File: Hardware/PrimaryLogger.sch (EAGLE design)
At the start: 91 parts, among them J1 CONN_42.54_SCREW, J2 CONN_42.54_SCREW, J3 CONN_42.54_SCREW, J4 CONN_42.54_SCREW, J5 CONN_32.54_SCREW, J9 GEMS_POWER_PLUGINPUT, Q1 DMG3404, Q2 DMG3404, U1 MIC2005, U10 TPL5010DDC, U11 MIC842, U12 PCA9617TSSOP8, U13 MCP23008SSOP, U2 MIC2005, U25 SN74AUP3G34DCU, U3 TPL5010DDC, U5 SN74LVC1G3157SC70, U6 TCS3400, U7 SHTC3DFN, U9 MCP7940SOIC

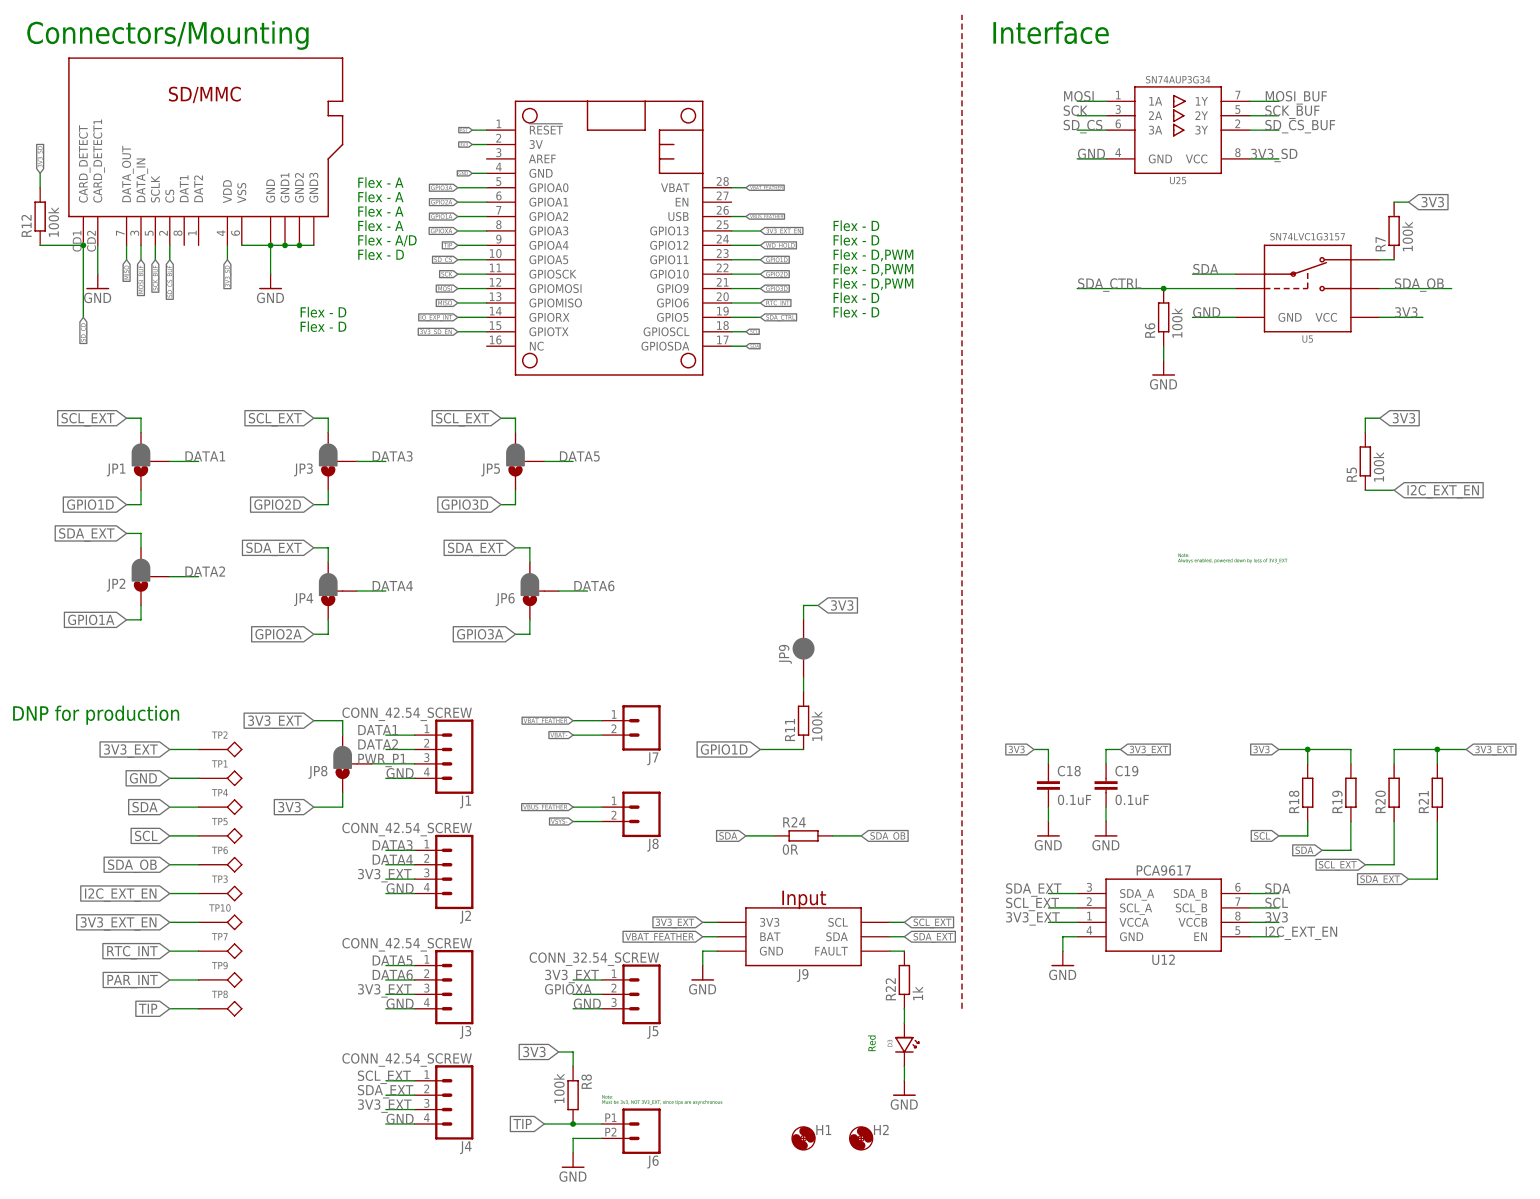
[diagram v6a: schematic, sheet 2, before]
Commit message: Cleanup and gerbers for v0.3A
Cleanup of schematic and layout for v0.3A design
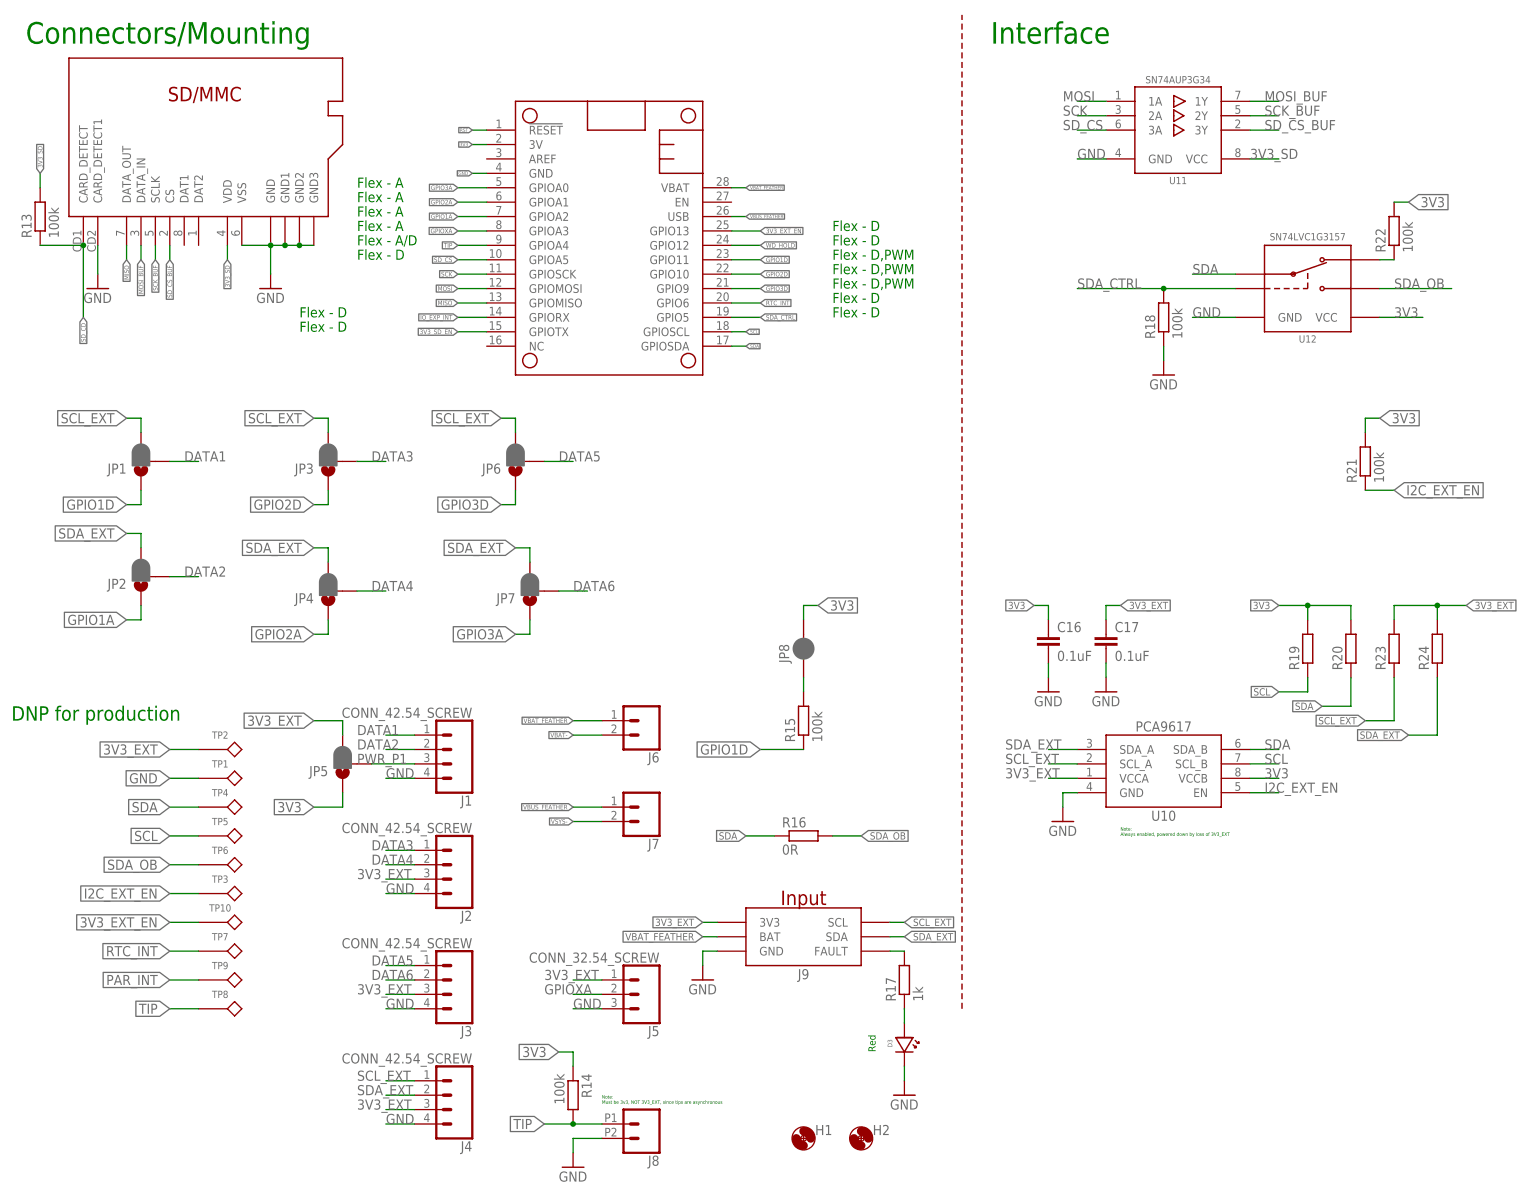
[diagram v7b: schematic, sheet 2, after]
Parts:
- removed C18, C19: 0.1uF, bschulz_passives:C-EU0.1UFC0603
- removed JP9: JUMPER-SMT_2_NC_PASTE_SILK, bschulz:JUMPER-SMT_2_NC_PASTE_SILK
- removed U13: MCP23008SSOP, bschulz:MCP23008SSOP
- removed U25: SN74AUP3G34DCU, bschulz:SN74AUP3G34DCU
- added C8, C9: 0.1uF, bschulz_passives:C-EU0.1UFC0603
- added JP7: JUMPER-SMT_3_1-NC_PASTE_SILK, bschulz:JUMPER-SMT_3_1-NC_PASTE_SILK
- added U4: SHTC3DFN, bschulz:SHTC3DFN
- added U8: MIC2005, bschulz:MIC2005
- C1, C2: value 6pF -> 0.1uF; device bschulz_passives:C-EU6PFC0402 -> bschulz_passives:C-EU0.1UFC0603
- C10: value 1uF -> 0.1uF; device bschulz_passives:C-EU1UFC0603 -> bschulz_passives:C-EU0.1UFC0603
- C11, C13, C14: value 0.1uF -> 10uF; device bschulz_passives:C-EU0.1UFC0603 -> bschulz_passives:C-EU10UFC0805
- C12: value 0.1uF -> 1uF; device bschulz_passives:C-EU0.1UFC0603 -> bschulz_passives:C-EU1UFC0603
- C5, C6: value 10uF -> 6pF; device bschulz_passives:C-EU10UFC0805 -> bschulz_passives:C-EU6PFC0402
- C7: value 10uF -> 0.1uF; device bschulz_passives:C-EU10UFC0805 -> bschulz_passives:C-EU0.1UFC0603
- J6: device bschulz:CONN_022.54_SCREW_ROUND -> bschulz:CONN_023.5MM_ROUND
- J8: device bschulz:CONN_023.5MM_ROUND -> bschulz:CONN_022.54_SCREW_ROUND
- JP8: value JUMPER-SMT_3_1-NC_PASTE_SILK -> JUMPER-SMT_2_NC_PASTE_SILK; device bschulz:JUMPER-SMT_3_1-NC_PASTE_SILK -> bschulz:JUMPER-SMT_2_NC_PASTE_SILK
- R10, R6, R9: value 100k -> 10k; device bschulz_passives:R-EU_100KR0603 -> bschulz_passives:R-EU_10KR0603
- R11, R12: value 100k -> 4.7k; device bschulz_passives:R-EU_100KR0603 -> bschulz_passives:R-EU_4.7KR0603
- R13, R15: value 10k -> 100k; device bschulz_passives:R-EU_10KR0603 -> bschulz_passives:R-EU_100KR0603
- R14: value 10k -> 100k
- R16: value 4.7k -> 0R; device bschulz_passives:R-EU_4.7KR0603 -> bschulz_passives:R-EU_R0603
- R17: value 4.7k -> 1k; device bschulz_passives:R-EU_4.7KR0603 -> bschulz_passives:R-EU_1KR0603
- R18, R21: value (none) -> 100k; device bschulz_passives:R-EU_4.7KR0603 -> bschulz_passives:R-EU_100KR0603
- R2: value 100k -> 0R; device bschulz_passives:R-EU_100KR0603 -> bschulz_passives:R-EU_R0603
- R22: value 1k -> 100k; device bschulz_passives:R-EU_1KR0603 -> bschulz_passives:R-EU_100KR0603
- R23, R24: value 0R -> (none); device bschulz_passives:R-EU_R0603 -> bschulz_passives:R-EU_4.7KR0603
- R8: device bschulz_passives:R-EU_10KR0603 -> bschulz_passives:R-EU_100KR0603
- U1: value MIC2005 -> MCP7940SOIC; device bschulz:MIC2005 -> bschulz:MCP7940SOIC
- U10: value TPL5010DDC -> PCA9617TSSOP8; device bschulz:TPL5010DDC -> bschulz:PCA9617TSSOP8
- U11: value MIC842 -> SN74AUP3G34DCU; device bschulz:MIC842 -> bschulz:SN74AUP3G34DCU
- U12: value PCA9617TSSOP8 -> SN74LVC1G3157SC70; device bschulz:PCA9617TSSOP8 -> bschulz:SN74LVC1G3157SC70
- U2: value MIC2005 -> TPL5010DDC; device bschulz:MIC2005 -> bschulz:TPL5010DDC
- U3: value TPL5010DDC -> MCP23008SSOP; device bschulz:TPL5010DDC -> bschulz:MCP23008SSOP
- U5: value SN74LVC1G3157SC70 -> TCS3400; device bschulz:SN74LVC1G3157SC70 -> bschulz:TCS3400
- U6: value TCS3400 -> TPL5010DDC; device bschulz:TCS3400 -> bschulz:TPL5010DDC
- U7: value SHTC3DFN -> MIC2005; device bschulz:SHTC3DFN -> bschulz:MIC2005
- U9: value MCP7940SOIC -> MIC842; device bschulz:MCP7940SOIC -> bschulz:MIC842
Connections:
- net 3V3: now also C2.1, C8.1, C9.1, JP5.1, JP8.2, R14.1, R2.2, R20.2, R21.2, R22.2, R8.2, U1.VCC, U10.VCCB, U12.VCC, U3.VDD, U4.VDD, U5.VDD, U7.VIN, U8.VIN, U9.VDD; no longer C17.1, C18.1, C6.1, JP8.1, JP9.2, R13.2, R18.2, R23.2, R3.2, R5.2, R8.1, U1.VIN, U10.VDD, U11.VDD, U12.VCCB, U13.VDD, U2.VIN, U5.VCC, U7.VDD, U9.VCC
- net 3V3_EXT: now also C14.1, C17.1, JP5.3, R23.2, R24.2, U10.VCCA, U7.VOUT; no longer C19.1, C7.1, JP8.3, R20.2, R21.2, U12.VCCA, U2.VOUT
- net 3V3_EXT_EN: now also R5.2, U7.EN; no longer R4.2, U2.EN
- net 3V3_EXT_FAULT: now also R7.1, U3.GP0, U7.!FAULT; no longer R3.1, U13.GP0, U2.!FAULT
- net 3V3_SD: now also C15.1, R13.2, U11.VCC, U8.VOUT; no longer C5.1, R12.2, U1.VOUT, U25.VCC
- net 3V3_SD_EN: now also R4.2, U8.EN; no longer R2.2, U1.EN
- net 3V3_SD_FAULT: now also R8.1, U3.GP1, U8.!FAULT; no longer R1.1, U1.!FAULT, U13.GP1
- net DATA5: now also JP6.2; no longer JP5.2
- net DATA6: now also JP7.2; no longer JP6.2
- net GND: now also C8.2, C9.2, J8.2, R18.1, R3.1, R5.1, U1.VSS, U3.A0, U3.A1, U3.A2, U3.VSS, U4.VSS, U6.DONE, U7.GND, U8.GND, U9.GND; no longer C18.2, C19.2, J6.2, R10.1, R14.1, R2.1, U1.GND, U10.DONE, U13.A0, U13.A1, U13.A2, U13.VSS, U25.GND, U3.GND, U7.VSS, U9.VSS
- net GPIO1D: now also R15.1; no longer R11.1
- net GPIO3A: now also JP7.1; no longer JP6.1
- net GPIO3D: now also JP6.1; no longer JP5.1
- net I2C_EXT_EN: now also R21.1, U10.EN, U3.GP3; no longer R5.1, U12.EN, U13.GP3
- net IO_EXP_INT: now also U3.INT; no longer U13.INT
- net MOSI: now also U11.1A; no longer U25.1A
- net MOSI_BUF: now also U11.1Y; no longer U25.1Y
- net N$1: now also C5.1, U1.X1; no longer C1.1, U9.X1
- net N$10: now also R11.2, R12.2, U9.OUT; no longer R16.2, R17.2, U11.OUT
- net N$11: now also R11.1; no longer R16.1
- net N$12: now also R12.1; no longer R17.1
- net N$13: now also R17.2; no longer R22.2
- net N$14: now also R17.1; no longer R22.1
- net N$2: now also C6.1, U1.X2; no longer C2.1, U9.X2
- net N$3: now also R3.2, U2.DELAY; no longer R10.2, U3.DELAY
- net N$4: now also R22.1, U12.B1; no longer R7.1, U5.B1
- net N$5: now also JP8.1, R15.2; no longer JP9.1, R11.2
- net N$6: now also C1.1, R2.1, U2.VDD; no longer C14.1, R23.1, U3.VDD
- net N$7: now also R6.2, U6.DELAY; no longer R14.2, U10.DELAY
- net N$8: now also C13.1, R10.2, U9.INP; no longer C15.1, R15.2, U11.INP
- net N$9: now also R10.1, R9.1, U6.RSTN; no longer R13.1, R15.1, U10.RSTN
- net PAR_INT: now also U3.GP4, U5.!INT; no longer U13.GP4, U6.!INT
- net PWR_P1: now also JP5.2; no longer JP8.2
- net RST: now also U2.RSTN, U3.!RESET; no longer U13.!RESET, U3.RSTN
- net RTC_INT: now also R1.1, U1.MFP; no longer R9.1, U9.MFP
- net SCK: now also U11.2A; no longer U25.2A
- net SCK_BUF: now also U11.2Y; no longer U25.2Y
- net SCL: now also R19.1, U1.SCL, U10.SCL_B, U3.SCL, U4.SCL, U5.SCL; no longer R18.1, U12.SCL_B, U13.SCL, U6.SCL, U7.SCL, U9.SCL
- net SCL_EXT: now also JP6.3, R23.1, U10.SCL_A; no longer JP5.3, R20.1, U12.SCL_A
- net SDA: now also R16.1, R20.1, U10.SDA_B, U12.A; no longer R19.1, R24.1, U12.SDA_B, U5.A
- net SDA_CTRL: now also R18.2, U12.S; no longer R6.2, U5.S
- net SDA_EXT: now also JP7.3, R24.1, U10.SDA_A; no longer JP6.3, R21.1, U12.SDA_A
- net SDA_OB: now also R16.2, U1.SDA, U12.B2, U3.SDA, U4.SDA, U5.SDA; no longer R24.2, U13.SDA, U5.B2, U6.SDA, U7.SDA, U9.SDA
- net SD_CD: now also R13.1, U3.GP2; no longer R12.1, U13.GP2
- net SD_CS: now also U11.3A; no longer U25.3A
- net SD_CS_BUF: now also U11.3Y; no longer U25.3Y
- net TIP: now also J8.1, R14.2; no longer J6.1, R8.2
- net VBAT: now also C7.1, U1.VBAT; no longer C13.1, U9.VBAT
- net VBAT-: now also J6.2; no longer J7.2
- net VBAT_FEATHER: now also J6.1; no longer J7.1
- net VBUS_FEATHER: now also J7.1; no longer J8.1
- net VSYS-: now also J7.2; no longer J8.2
- net WAKE: now also U2.WAKE, U3.GP5; no longer U13.GP5, U3.WAKE
- net WD_HOLD: now also U2.DONE; no longer U3.DONE
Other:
- moved on the sheet: C1, C10, C11, C12, C13, C14, C15, C2, C3, C4, C5, C6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
